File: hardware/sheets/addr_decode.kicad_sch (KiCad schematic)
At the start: 22 parts, among them U1 74HC138, U2 74HC00, U3 74HC32, U4 74HC32, U5 74LVC125A

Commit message: addr_decode: hardwire LPT/IDE bases; centralize NIC + video disables (JP1-JP6)
LPT fixed at 0x378, IDE at 0x300 -- both base straps and their pull-ups
deleted ('138 ~Y1 now NC, the '00's ~A5 gate spare, IDE OR-leg takes raw
A5). The NIC and video disable jumpers move to addr_decode as JP5/JP6
with the same fit-to-disable sense as the rest: their gating hardware
stays local (the NIC's isolation '125 inside the 5V island, video's
firmware boot strap on GPIO42), only the jumper levels cross as
mxbus.PRIV_DIS -- video's documented firmware polarity inverts (high =
disabled; no firmware exists yet). Disable row is now a uniform JP1-JP6
(COM1/COM2/LPT/IDE/NIC/VID), bare board runs everything; network JP1/R6
and video JP1/R30 deleted, VID_BASE becomes video JP1. card_video's
wrapper re-adds a local DIS_VID strap (the documented PRIV lift
pattern). Docs/tables/decision logs aligned.

Co-Authored-By: Claude Fable 5 <noreply@anthropic.com>
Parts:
- removed JP1: LPT 378/278, Connector_PinHeader_2.54mm:PinHeader_1x03_P2.54mm_Vertical, symbol Connector_Generic:Conn_01x03
- removed JP2: IDE 300/320, Connector_PinHeader_2.54mm:PinHeader_1x03_P2.54mm_Vertical, symbol Connector_Generic:Conn_01x03
- added JP1: DIS COM1, Connector_PinHeader_2.54mm:PinHeader_1x02_P2.54mm_Vertical, symbol Connector_Generic:Conn_01x02
- added R1: 10k, Resistor_SMD:R_0603_1608Metric, symbol Device:R
- JP2: renamed from R1; value 10k -> DIS COM2; footprint Resistor_SMD:R_0603_1608Metric -> Connector_PinHeader_2.54mm:PinHeader_1x02_P2.54mm_Vertical; symbol Device:R -> Connector_Generic:Conn_01x02; LCSC Part Num C25804 -> C2337
- JP3: value DIS COM1 -> DIS LPT
- JP4: value DIS COM2 -> DIS IDE
- JP5: value DIS LPT -> DIS NIC
- JP6: value DIS IDE -> DIS VID
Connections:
- net WIN_LPT378 is gone; now on net WIN_LPT: U1.10 (~{Y5})
- net +3V3: now also JP2.2 (Pin_2), JP1.2 (Pin_2); no longer JP2.1, R2.1
- net A5: now also U3.13 (P13); no longer U2.12 (P12), U2.13 (P13)
- net DIS_COM1: now also JP1.1 (Pin_1), R1.1; no longer JP3.1 (Pin_1), R3.1
- net DIS_COM2: now also JP2.1 (Pin_1), R2.1; no longer JP4.1 (Pin_1), R4.1
- net DIS_IDE: now also JP4.1 (Pin_1), R4.1; no longer JP6.1 (Pin_1), R6.1
- net DIS_LPT: now also JP3.1 (Pin_1), R3.1; no longer JP5.1 (Pin_1), R5.1
- net GND: now also R2.2, U2.12 (P12), U2.13 (P13), R1.2
- net A5_N: no longer names the net of U2.11 (P11)
- removed net IDE_A5: R2.2, U3.13 (P13)
- net LPT_WIN renamed WIN_LPT
- net WIN_LPT: no longer JP2.2
- net WIN_LPT278: no longer names the net of U1.14 (~{Y1})
- new net DIS_NIC: JP5.1 (Pin_1), R5.1
- new net DIS_VID: JP6.1 (Pin_1), R6.1
- no-connect marks 3 -> 5
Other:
- note added: "JP1-JP6 (COM1/COM2/LPT/IDE/NIC/VID): peripheral ENABLED by default; fit jumper to disable (kills decode/IRQ, frees the slot)"
- note added: "One decode for all discrete peripherals, bases hardwired: COM1 0x3F8, COM2 0x2F8, LPT 0x378, IDE 0x300"
- note removed: "JP3-JP6: peripheral ENABLED by default; fit jumper to disable (kills decode, silences IRQ, frees address+IRQ for expansion)"
- note removed: "One decode for all discrete peripherals: COM1 0x3F8, COM2 0x2F8, LPT JP1 0x378/0x278, IDE JP2 0x300/0x320"
- moved on the sheet: JP3, JP4, JP5, JP6, R2, R3, R4, R5, R6

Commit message: Passives: basic-library audit + 4x resistor-array pull consolidation
Audit: every discrete R/C value was already JLC basic except the ferrite
beads -- swapped to basic Murata BLM18PG121SN1D (C14709, 120R@100MHz,
same family/role). The 100uF electrolytic and buck inductor stay
extended (zero fee-free parts exist in those subcategories). Pruned the
orphaned 5V-era 47nF/330nF MAX3241 cap entries.

Pull consolidation: 65 discrete 10k/4.7k rail pulls across 8 sheets
collapse into 18 basic 4-element isolated arrays (4D03WGJ0103T5E /
4D03WGJ0472T5E, element k = pins k/9-k; new mxbus.r_pack4 helper).
Isolated elements let packs mix rails; every net keeps its exact rail
and semantics (verified element-by-element in the netlist). RC/divider/
series/I2C resistors stay discrete. Board 452 -> 406 components; also
de-risks the sole basic 10k 0603 line (0 stock at audit). Audit
recorded in jlcpcb-sourcing.md.

Co-Authored-By: Claude Fable 5 <noreply@anthropic.com>
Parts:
- removed JP5: DIS NIC, Connector_PinHeader_2.54mm:PinHeader_1x02_P2.54mm_Vertical, symbol Connector_Generic:Conn_01x02
- removed JP6: DIS VID, Connector_PinHeader_2.54mm:PinHeader_1x02_P2.54mm_Vertical, symbol Connector_Generic:Conn_01x02
- removed R4, R5, R6: 10k, Resistor_SMD:R_0603_1608Metric, symbol Device:R
- added RN2: 10kx4, Resistor_SMD:R_Array_Convex_4x0603, symbol Device:R_Pack04
- JP2: renamed from R1; value 10k -> DIS COM2; footprint Resistor_SMD:R_0603_1608Metric -> Connector_PinHeader_2.54mm:PinHeader_1x02_P2.54mm_Vertical; symbol Device:R -> Connector_Generic:Conn_01x02; LCSC Part Num C25804 -> C2337
- JP3: renamed from JP2; value DIS COM2 -> DIS LPT
- JP4: renamed from R2; value 10k -> DIS IDE; footprint Resistor_SMD:R_0603_1608Metric -> Connector_PinHeader_2.54mm:PinHeader_1x02_P2.54mm_Vertical; symbol Device:R -> Connector_Generic:Conn_01x02; LCSC Part Num C25804 -> C2337
- JP5: renamed from JP3; value DIS LPT -> DIS NIC
- JP6: renamed from R3; value 10k -> DIS VID; footprint Resistor_SMD:R_0603_1608Metric -> Connector_PinHeader_2.54mm:PinHeader_1x02_P2.54mm_Vertical; symbol Device:R -> Connector_Generic:Conn_01x02; LCSC Part Num C25804 -> C2337
- RN1: renamed from JP4; value DIS IDE -> 10kx4; footprint Connector_PinHeader_2.54mm:PinHeader_1x02_P2.54mm_Vertical -> Resistor_SMD:R_Array_Convex_4x0603; symbol Connector_Generic:Conn_01x02 -> Device:R_Pack04; LCSC Part Num C2337 -> C29718
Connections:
- net +3V3: now also JP2.2 (Pin_2), JP4.2 (Pin_2), JP6.2 (Pin_2); no longer RN1.2 (Pin_2)
- net DIS_COM1: now also RN1.1 (R1.1); no longer JP2.1
- net DIS_COM2: now also JP2.1 (Pin_1), RN1.2 (R2.1); no longer JP3.1 (Pin_1), JP4.1
- net DIS_IDE: now also JP4.1 (Pin_1), RN1.4 (R4.1); no longer RN1.1 (Pin_1)
- net DIS_LPT: now also JP3.1 (Pin_1), RN1.3 (R3.1); no longer JP5.1 (Pin_1), JP6.1
- net DIS_NIC: now also JP5.1 (Pin_1), RN2.1 (R1.1)
- net DIS_VID: now also JP6.1 (Pin_1), RN2.2 (R2.1)
- net GND: now also RN1.5 (R4.2), RN1.6 (R3.2), RN1.7 (R2.2), RN1.8 (R1.2), RN2.7 (R2.2), RN2.8 (R1.2); no longer JP2.2, JP4.2, JP6.2
- no-connect marks 5 -> 9
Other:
- moved on the sheet: JP3, JP5

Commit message: Remove the on-board RTL8019AS NIC (tag full-board-with-nic preserves it)
Network sheet, symbols, and NIC-only parts.py bindings deleted; addr_decode
JP6->JP5 (DIS_VID); IRQ2 retired as an internal net like IRQ6/IRQ8 (still
reachable as EXT_IRQ2 from the expansion port). ERC stays 0/0.

Co-Authored-By: Claude Fable 5 <noreply@anthropic.com>
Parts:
- removed C4, C5: 100nF, Capacitor_SMD:C_0603_1608Metric, symbol Device:C
- removed JP6: DIS VID, Connector_PinHeader_2.54mm:PinHeader_1x02_P2.54mm_Vertical, symbol Connector_Generic:Conn_01x02
- added C1, C2: 100nF, Capacitor_SMD:C_0603_1608Metric, symbol Device:C
- JP5: value DIS NIC -> DIS VID
- renumbered C1 to C3, C2 to C4, C3 to C5
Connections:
- net DIS_NIC is gone; now on net DIS_VID: JP5.1 (Pin_1), RN2.1 (R1.1)
- net +3V3: now also C1.1, C2.1
- net DIS_VID: no longer RN2.2 (R2.1)
- net GND: now also C1.2, C2.2; no longer RN2.7 (R2.2)
- no-connect marks 9 -> 11
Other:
- note added: "JP1-JP5 (COM1/COM2/LPT/IDE/VID): peripheral ENABLED by default; fit jumper to disable (kills decode/IRQ, frees the slot)"
- note removed: "JP1-JP6 (COM1/COM2/LPT/IDE/NIC/VID): peripheral ENABLED by default; fit jumper to disable (kills decode/IRQ, frees the slot)"
- moved on the sheet: C3, C4, C5
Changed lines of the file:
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@@
 		)
 	)
-	(label "DIS_NIC"
+	(label "DIS_VID"
 		(at 22.86 71.12 180)
 		(effects
@@
 		)
 	)
-	(hierarchical_label "DIS_NIC"
+	(hierarchical_label "DIS_VID"
 		(shape output)
 		(at 25.4 71.12 0)
@@
 		)
 	)
-	(label "DIS_VID"
+	(label "IRQ4"
 		(at 22.86 73.66 180)
 		(effects
@@
 		)
 	)
-	(hierarchical_label "DIS_VID"
+	(hierarchical_label "IRQ4"
 		(shape output)
 		(at 25.4 73.66 0)
@@
 		)
 	)
-	(label "IRQ4"
+	(label "IRQ3"
 		(at 22.86 76.2 180)
 		(effects
@@
 		)
 	)
-	(hierarchical_label "IRQ4"
+	(hierarchical_label "IRQ3"
 		(shape output)
 		(at 25.4 76.2 0)
@@
 		)
 	)
-	(label "IRQ3"
+	(label "IRQ7"
 		(at 22.86 78.74 180)
 		(effects
@@
 		)
 	)
-	(hierarchical_label "IRQ3"
+	(hierarchical_label "IRQ7"
 		(shape output)
 		(at 25.4 78.74 0)
@@
 		)
 	)
-	(label "IRQ7"
-		(at 22.86 81.28 180)
-		(effects
-			(font
-				(size 1.27 1.27)
-			)
-			(justify right)
-		)
-	)
-	(hierarchical_label "IRQ7"
-		(shape output)
-		(at 25.4 81.28 0)
-		(effects
-			(font
-				(size 1.27 1.27)
-			)
-		)
-	)
-	(wire
-		(pts
-			(xy 22.86 83.82)
-			(xy 25.4 83.82)
-		)
-		(stroke
-			(width 0)
-			(type default)
-		)
-	)
 	(label "IRQ14"
-		(at 22.86 83.82 180)
+		(at 22.86 81.28 180)
 		(effects
 			(font
@@
 	(hierarchical_label "IRQ14"
 		(shape output)
-		(at 25.4 83.82 0)
+		(at 25.4 81.28 0)
 		(effects
 			(font
@@
 		)
 	)
-	(label "DIS_NIC"
+	(label "DIS_VID"
 		(at 200.66 177.8 0)
 		(effects
@@
 	(wire
 		(pts
-			(xy 248.92 177.8)
-			(xy 251.46 177.8)
-		)
-		(stroke
-			(width 0)
-			(type default)
-		)
-	)
-	(label "DIS_VID"
-		(at 251.46 177.8 0)
-		(effects
-			(font
-				(size 1.27 1.27)
-			)
-		)
-	)
-	(wire
-		(pts
-			(xy 248.92 180.34)
-			(xy 251.46 180.34)
-		)
-		(stroke
-			(width 0)
-			(type default)
-		)
-	)
-	(global_label "+3V3"
-		(shape input)
-		(at 251.46 180.34 0)
-		(effects
-			(font
-				(size 1.27 1.27)
-			)
-		)
-	)
-	(wire
-		(pts
 			(xy 393.7 157.48)
 			(xy 393.7 160.02)
@@
 		)
 	)
-	(label "DIS_NIC"
+	(label "DIS_VID"
 		(at 393.7 185.42 270)
 		(effects
@@
 		)
 	)
-	(wire
-		(pts
-			(xy 396.24 182.88)
-			(xy 396.24 185.42)
-		)
-		(stroke
-			(width 0)
-			(type default)
-		)
-	)
-	(label "DIS_VID"
-		(at 396.24 185.42 270)
-		(effects
-			(font
-				(size 1.27 1.27)
-			)
-		)
-	)
-	(wire
-		(pts
-			(xy 396.24 172.72)
-			(xy 396.24 170.18)
-		)
-		(stroke
-			(width 0)
-			(type default)
-		)
+	(no_connect
+		(at 396.24 182.88)
 	)
-	(global_label "GND"
-		(shape input)
-		(at 396.24 170.18 90)
-		(effects
-			(font
-				(size 1.27 1.27)
-			)
-		)
+	(no_connect
+		(at 396.24 172.72)
 	)
 	(no_connect
@@
 		)
 	)
-	(text "JP1-JP6 (COM1/COM2/LPT/IDE/NIC/VID): peripheral ENABLED by default; fit jumper to disable (kills decode/IRQ, frees the slot)"
+	(text "JP1-JP5 (COM1/COM2/LPT/IDE/VID): peripheral ENABLED by default; fit jumper to disable (kills decode/IRQ, frees the slot)"
 		(at 101.6 213.36 0)
 		(effects
@@
 		(instances
 			(project "mini-xt"
-				(path "/26736c46-8b40-5460-874f-03596d17270c/e1358770-8f2b-55db-b539-0c522cf40ecb"
-					(reference "U1301")
+				(path "/26736c46-8b40-5460-874f-03596d17270c/48c0b311-cc4d-54d9-83db-6f9ac2b0230b"
+					(reference "U1201")
 					(unit 1)
 				)
@@
 		(instances
 			(project "mini-xt"
-				(path "/26736c46-8b40-5460-874f-03596d17270c/e1358770-8f2b-55db-b539-0c522cf40ecb"
-					(reference "U1302")
+				(path "/26736c46-8b40-5460-874f-03596d17270c/48c0b311-cc4d-54d9-83db-6f9ac2b0230b"
+					(reference "U1202")
 					(unit 1)
 				)
@@
 		(instances
 			(project "mini-xt"
-				(path "/26736c46-8b40-5460-874f-03596d17270c/e1358770-8f2b-55db-b539-0c522cf40ecb"
-					(reference "U1303")
+				(path "/26736c46-8b40-5460-874f-03596d17270c/48c0b311-cc4d-54d9-83db-6f9ac2b0230b"
+					(reference "U1203")
 					(unit 1)
 				)
@@
 		(instances
 			(project "mini-xt"
-				(path "/26736c46-8b40-5460-874f-03596d17270c/e1358770-8f2b-55db-b539-0c522cf40ecb"
-					(reference "U1304")
+				(path "/26736c46-8b40-5460-874f-03596d17270c/48c0b311-cc4d-54d9-83db-6f9ac2b0230b"
+					(reference "U1204")
 					(unit 1)
 				)
@@
 		(instances
 			(project "mini-xt"
-				(path "/26736c46-8b40-5460-874f-03596d17270c/e1358770-8f2b-55db-b539-0c522cf40ecb"
-					(reference "U1305")
+				(path "/26736c46-8b40-5460-874f-03596d17270c/48c0b311-cc4d-54d9-83db-6f9ac2b0230b"
+					(reference "U1205")
 					(unit 1)
 				)
@@
 		(instances
 			(project "mini-xt"
-				(path "/26736c46-8b40-5460-874f-03596d17270c/e1358770-8f2b-55db-b539-0c522cf40ecb"
-					(reference "JP1301")
+				(path "/26736c46-8b40-5460-874f-03596d17270c/48c0b311-cc4d-54d9-83db-6f9ac2b0230b"
+					(reference "JP1201")
 					(unit 1)
 				)
@@
 		(instances
 			(project "mini-xt"
-				(path "/26736c46-8b40-5460-874f-03596d17270c/e1358770-8f2b-55db-b539-0c522cf40ecb"
-					(reference "JP1302")
+				(path "/26736c46-8b40-5460-874f-03596d17270c/48c0b311-cc4d-54d9-83db-6f9ac2b0230b"
+					(reference "JP1202")
 					(unit 1)
 				)
@@
 		(instances
 			(project "mini-xt"
-				(path "/26736c46-8b40-5460-874f-03596d17270c/e1358770-8f2b-55db-b539-0c522cf40ecb"
-					(reference "JP1303")
+				(path "/26736c46-8b40-5460-874f-03596d17270c/48c0b311-cc4d-54d9-83db-6f9ac2b0230b"
+					(reference "JP1203")
 					(unit 1)
 				)
@@
 		(instances
 			(project "mini-xt"
-				(path "/26736c46-8b40-5460-874f-03596d17270c/e1358770-8f2b-55db-b539-0c522cf40ecb"
-					(reference "JP1304")
+				(path "/26736c46-8b40-5460-874f-03596d17270c/48c0b311-cc4d-54d9-83db-6f9ac2b0230b"
+					(reference "JP1204")
 					(unit 1)
 				)
@@
 			)
 		)
-		(property "Value" "DIS NIC"
+		(property "Value" "DIS VID"
 			(at 203.2 182.88 0)
 			(effects
@@
 		(instances
 			(project "mini-xt"
-				(path "/26736c46-8b40-5460-874f-03596d17270c/e1358770-8f2b-55db-b539-0c522cf40ecb"
-					(reference "JP1305")
-					(unit 1)
-				)
-			)
-		)
-	)
-	(symbol
-		(lib_id "Connector_Generic:Conn_01x02")
-		(at 254 177.8 0)
-		(unit 1)
-		(exclude_from_sim no)
-		(in_bom yes)
-		(on_board yes)
-		(dnp no)
-		(fields_autoplaced yes)
-		(property "Reference" "JP6"
-			(at 254 172.72 0)
-			(effects
-				(font
-					(size 1.27 1.27)
-				)
-			)
-		)
-		(property "Value" "DIS VID"
-			(at 254 182.88 0)
-			(effects
-				(font
-					(size 1.27 1.27)
-				)
-			)
-		)
-		(property "Footprint" "Connector_PinHeader_2.54mm:PinHeader_1x02_P2.54mm_Vertical"
-			(at 254 177.8 0)
-			(effects
-				(font
-					(size 1.27 1.27)
-				)
-				(hide yes)
-			)
-		)
-		(property "LCSC Part Num" "C2337"
-			(at 254 177.8 0)
-			(effects
-				(font
-					(size 1.27 1.27)
-				)
-				(hide yes)
-			)
-		)
-		(pin "1"
-		)
-		(pin "2"
-		)
-		(instances
-			(project "mini-xt"
-				(path "/26736c46-8b40-5460-874f-03596d17270c/e1358770-8f2b-55db-b539-0c522cf40ecb"
-					(reference "JP1306")
+				(path "/26736c46-8b40-5460-874f-03596d17270c/48c0b311-cc4d-54d9-83db-6f9ac2b0230b"
+					(reference "JP1205")
 					(unit 1)
 				)
@@
 		(instances
 			(project "mini-xt"
-				(path "/26736c46-8b40-5460-874f-03596d17270c/e1358770-8f2b-55db-b539-0c522cf40ecb"
-					(reference "RN1301")
+				(path "/26736c46-8b40-5460-874f-03596d17270c/48c0b311-cc4d-54d9-83db-6f9ac2b0230b"
+					(reference "RN1201")
 					(unit 1)
 				)
@@
 		(instances
 			(project "mini-xt"
-				(path "/26736c46-8b40-5460-874f-03596d17270c/e1358770-8f2b-55db-b539-0c522cf40ecb"
-					(reference "RN1302")
+				(path "/26736c46-8b40-5460-874f-03596d17270c/48c0b311-cc4d-54d9-83db-6f9ac2b0230b"
+					(reference "RN1202")
 					(unit 1)
 				)
@@
 		(instances
 			(project "mini-xt"
-				(path "/26736c46-8b40-5460-874f-03596d17270c/e1358770-8f2b-55db-b539-0c522cf40ecb"
-					(reference "C1301")
+				(path "/26736c46-8b40-5460-874f-03596d17270c/48c0b311-cc4d-54d9-83db-6f9ac2b0230b"
+					(reference "C1201")
 					(unit 1)
 				)
@@
 		(instances
 			(project "mini-xt"
-				(path "/26736c46-8b40-5460-874f-03596d17270c/e1358770-8f2b-55db-b539-0c522cf40ecb"
-					(reference "C1302")
+				(path "/26736c46-8b40-5460-874f-03596d17270c/48c0b311-cc4d-54d9-83db-6f9ac2b0230b"
+					(reference "C1202")
 					(unit 1)
 				)
@@
 		(instances
 			(project "mini-xt"
-				(path "/26736c46-8b40-5460-874f-03596d17270c/e1358770-8f2b-55db-b539-0c522cf40ecb"
-					(reference "C1303")
+				(path "/26736c46-8b40-5460-874f-03596d17270c/48c0b311-cc4d-54d9-83db-6f9ac2b0230b"
+					(reference "C1203")
 					(unit 1)
 				)
@@
 		(instances
 			(project "mini-xt"
-				(path "/26736c46-8b40-5460-874f-03596d17270c/e1358770-8f2b-55db-b539-0c522cf40ecb"
-					(reference "C1304")
+				(path "/26736c46-8b40-5460-874f-03596d17270c/48c0b311-cc4d-54d9-83db-6f9ac2b0230b"
+					(reference "C1204")
 					(unit 1)
 				)
@@
 		(instances
 			(project "mini-xt"
-				(path "/26736c46-8b40-5460-874f-03596d17270c/e1358770-8f2b-55db-b539-0c522cf40ecb"
-					(reference "C1305")
+				(path "/26736c46-8b40-5460-874f-03596d17270c/48c0b311-cc4d-54d9-83db-6f9ac2b0230b"
+					(reference "C1205")
 					(unit 1)
 				)

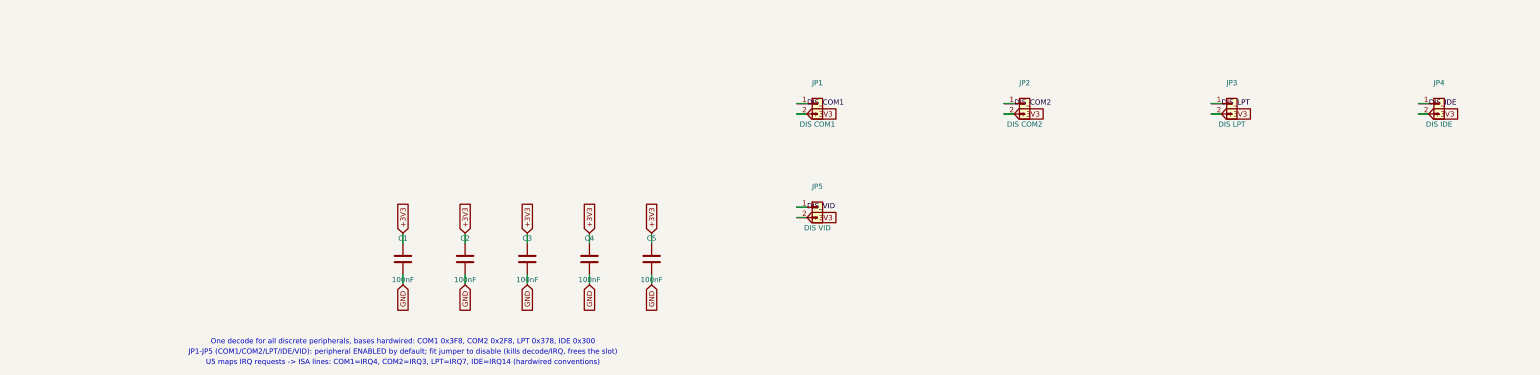
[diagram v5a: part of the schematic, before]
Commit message: Expansion port: 50-pin header, port DMA channel, dev cards deleted
Two waves of the 2026-07-14/15 expansion-port rework (the first was
uncommitted): the IRQ-scan collapse to one '165 + '32 OR rank with
ISA-card DMA removed outright, then the port redesign that brings one
DMA channel back:

- isa_conn: 60-pin (2x30, PicoGUS-standard layout) -> 50-pin (2x25,
  project-private pinout; 50-way IDC is far easier to source). OSC and
  ~REFRESH dropped to fit (no on-board consumer / no DRAM refresh; the
  planned ISA backplane board re-creates both for period cards).
- Port DMA: EXT_DRQ rides the sidecar inbound '244 + U12 '165 spare D6
  lane (zero GPIO); ~EXT_DACK = GPIO47 (freed by ~REFRESH) out through
  the strobe '244. Separate nets from the internal PicoGUS pair, so a
  port card never sees the on-board acknowledge.
- DRQ1/~DACK1 renamed DRQ/~DACK (ch2/3 long retired); DRQ2/3 +
  ~DACK2/3 removed from the mxbus contract.
- card_video + card_isatest deleted (sheets, hardware/cards/,
  build_cards()); superseded by the backplane plan. History has them.
- Connector parts: IDE header -> shrouded 2x20 IDC box (C9138, keypin
  20 NC'd); expansion port -> 90-degree 2x25 female socket (C21262364);
  addr_decode's five disable jumpers folded into ONE fixed 2x5 block
  JP1 (C492422), positions JP1.1-JP1.5 = COM1/COM2/LPT/IDE/VID.

ERC 0/0, check_parts 0 problems; docs/notes updated throughout.

Co-Authored-By: Claude Fable 5 <noreply@anthropic.com>
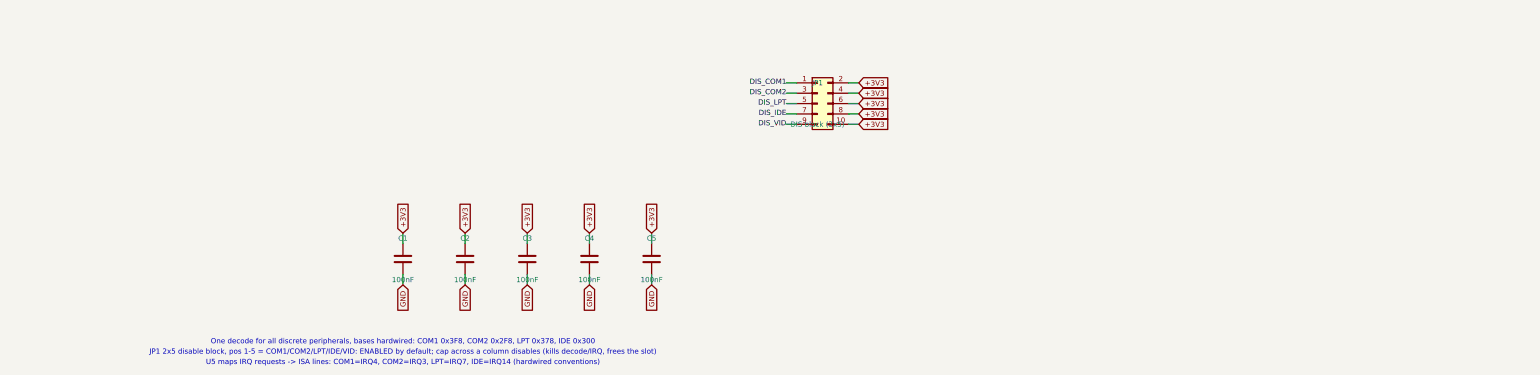
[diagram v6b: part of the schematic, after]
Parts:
- removed JP2: DIS COM2, Connector_PinHeader_2.54mm:PinHeader_1x02_P2.54mm_Vertical, symbol Connector_Generic:Conn_01x02
- removed JP3: DIS LPT, Connector_PinHeader_2.54mm:PinHeader_1x02_P2.54mm_Vertical, symbol Connector_Generic:Conn_01x02
- removed JP4: DIS IDE, Connector_PinHeader_2.54mm:PinHeader_1x02_P2.54mm_Vertical, symbol Connector_Generic:Conn_01x02
- removed JP5: DIS VID, Connector_PinHeader_2.54mm:PinHeader_1x02_P2.54mm_Vertical, symbol Connector_Generic:Conn_01x02
- JP1: value DIS COM1 -> DIS block (2x5); footprint Connector_PinHeader_2.54mm:PinHeader_1x02_P2.54mm_Vertical -> Connector_PinHeader_2.54mm:PinHeader_2x05_P2.54mm_Vertical; symbol Connector_Generic:Conn_01x02 -> Connector_Generic:Conn_02x05_Odd_Even; LCSC Part Num C2337 -> C492422
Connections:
- net +3V3: now also JP1.10 (Pin_10), JP1.4 (Pin_4), JP1.6 (Pin_6), JP1.8 (Pin_8)
- net DIS_COM2: now also JP1.3 (Pin_3)
- net DIS_IDE: now also JP1.7 (Pin_7)
- net DIS_LPT: now also JP1.5 (Pin_5)
- net DIS_VID: now also JP1.9 (Pin_9)
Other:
- note added: "JP1 2x5 disable block, pos 1-5 = COM1/COM2/LPT/IDE/VID: ENABLED by default; cap across a column disables (kills decode/IRQ, frees the slot)"
- note removed: "JP1-JP5 (COM1/COM2/LPT/IDE/VID): peripheral ENABLED by default; fit jumper to disable (kills decode/IRQ, frees the slot)"
